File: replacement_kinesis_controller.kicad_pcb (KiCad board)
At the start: 2 copper layers, 99.1 x 99.1 mm, 138 parts, among them CN1 USB_general, CN2 Micro-USB, CN3 Mini-USB, CN4 USB_general, K1 CONN_3, K2 CONN_3, K3 CONN_3, K4 CONN_3, K5 CONN_3, P1 CONN_3X2, P10 CONN_8, P11 CONN_5, P12 CONN_5, P13 CONN_6, P14 CONN_8, P15 CONN_5X2, P16 CONN_16, P17 CONN_16, P18 POWER, P19 PCM, P2 CONN_13, P20 UART, P21 SPI, P22 IO, P23 SMIRF, P24 CONN_2, P25 USB, P3 CONN_13, P4 CONN_10, P5 CONN_10, P6 CONN_13, P7 CONN_13, P8 CONN_5X2, P9 CONN_6, Q1 MOS_P, Q2 MOS_N, Q3 MOS_P, SW1 SW_PUSH, SW2 SW_PUSH, SW3 SPST, SW4 SPST, U1 MCP23018-E, U2 WS2811_RGB_LED, U3 WS2811_RGB_LED, U4 WS2811_RGB_LED, U5 WS2811_RGB_LED, U6 ATmega32U4, U7 WT12-A, U8 MCP73832, U9 MIC5504, X1 16MHz

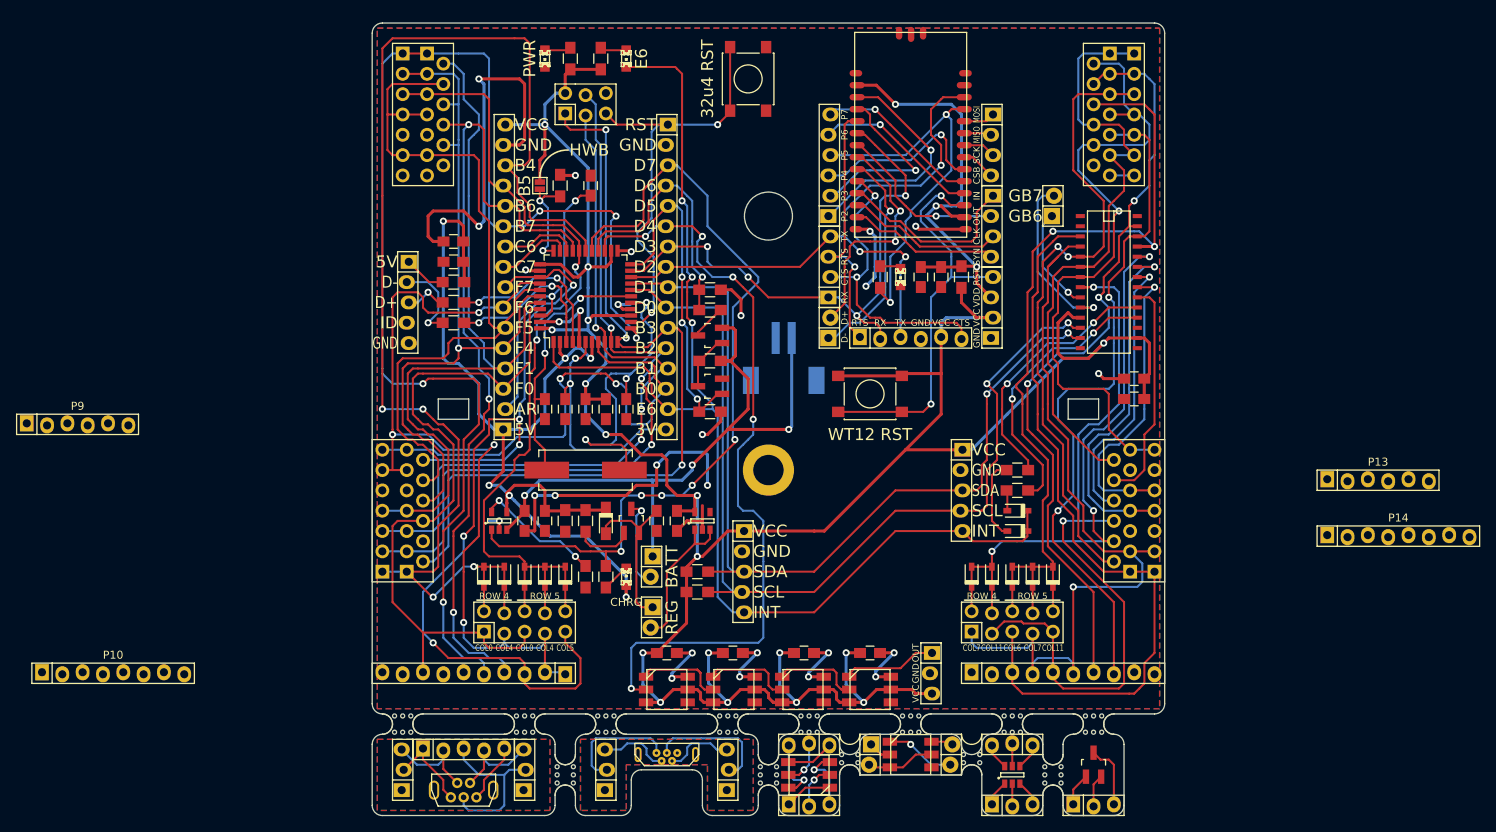
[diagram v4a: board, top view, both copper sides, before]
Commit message: Rejigger things to make board more easily separable
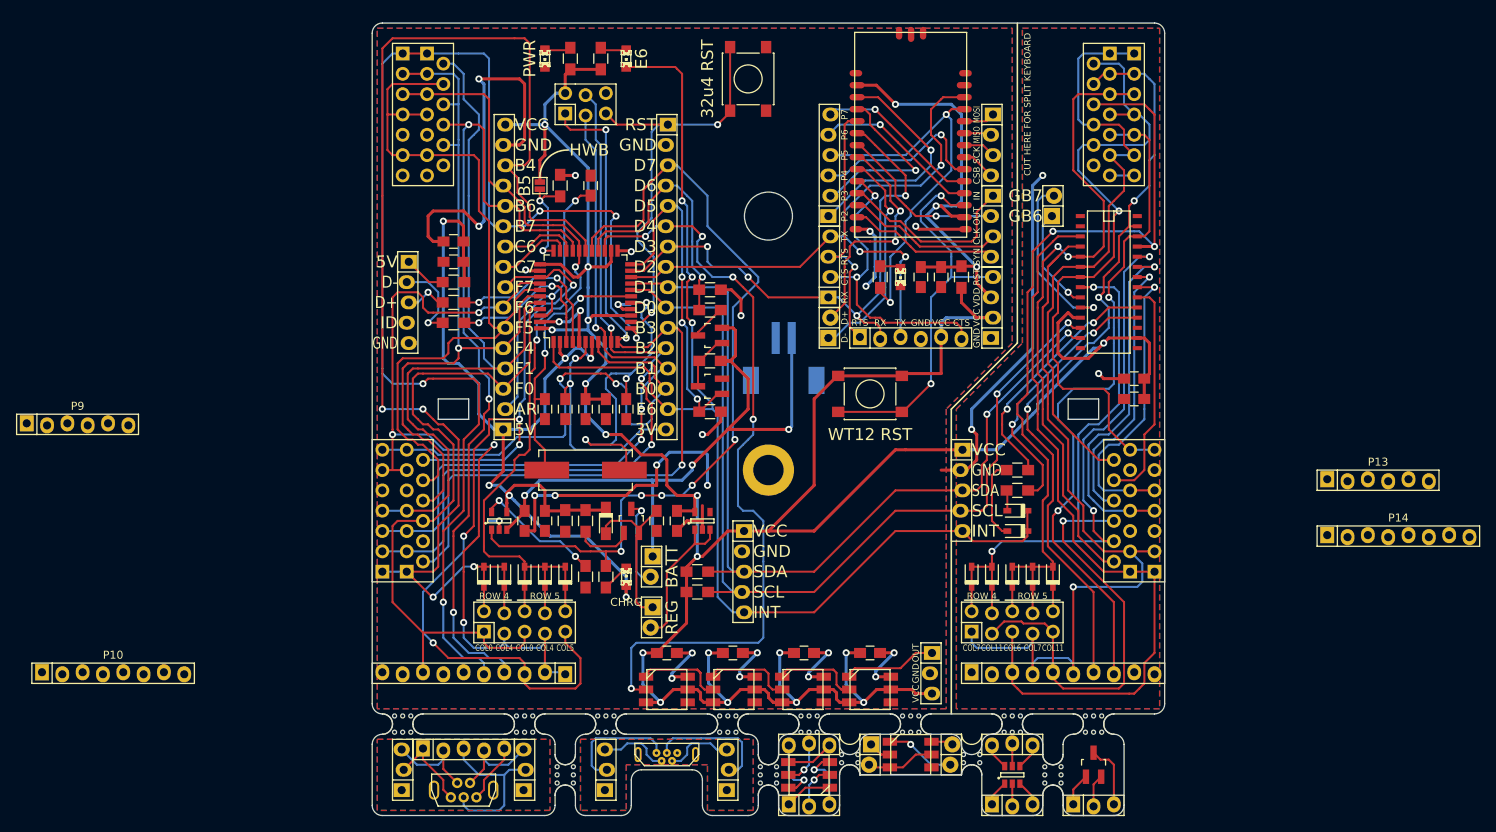
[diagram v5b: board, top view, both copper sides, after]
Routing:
- net GND: track 169.0 -> 213.5 mm, vias 27 -> 29
- net VCC: track 352.5 -> 364.6 mm
- net PD0: track 120.0 -> 117.5 mm
- net SDA: track 114.7 -> 113.2 mm
- net GPA7: track 96.7 -> 95.2 mm
- net W_RESET: track 51.6 -> 50.1 mm
- net INTB: track 35.0 -> 33.5 mm
- net INTA: track 32.6 -> 31.1 mm
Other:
- board text added: "CUT HERE FOR SPLIT KEYBOARD"

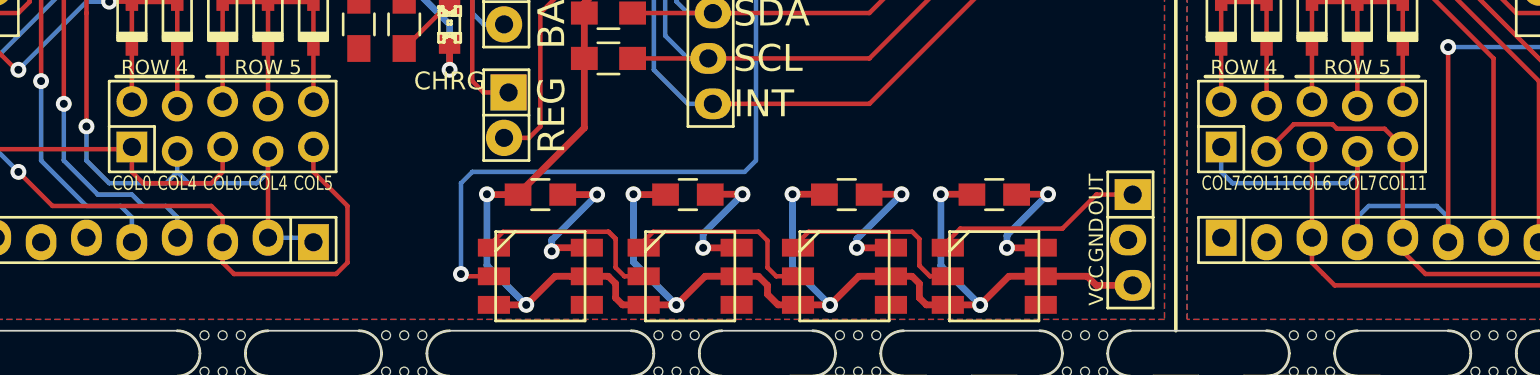
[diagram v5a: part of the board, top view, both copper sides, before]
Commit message: A bunch of silkscreen improvements
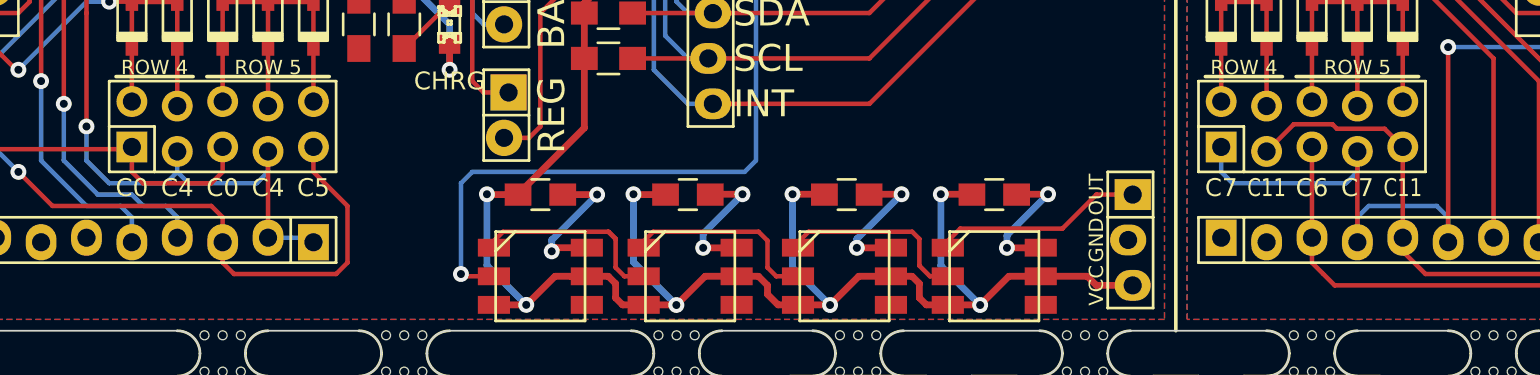
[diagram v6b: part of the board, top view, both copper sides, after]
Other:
- board text added: "C0"
- board text added: "C11"
- board text added: "C4"
- board text added: "C5"
- board text removed: "COL0"
- board text removed: "COL11"
- board text removed: "COL4"
- board text removed: "COL5"
- board text removed: "COL6"
- board text removed: "COL7"

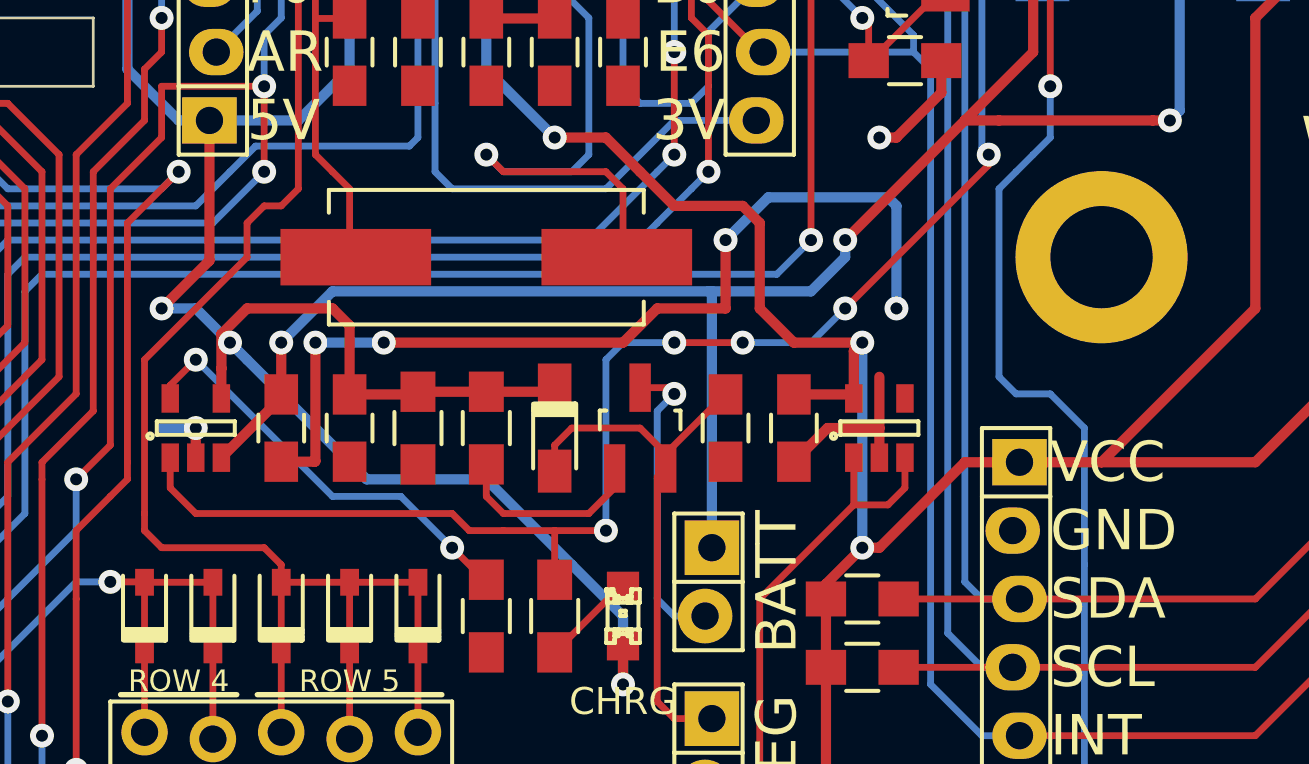
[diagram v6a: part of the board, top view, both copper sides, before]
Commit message: Update sot23-5 footprint for handsoldering
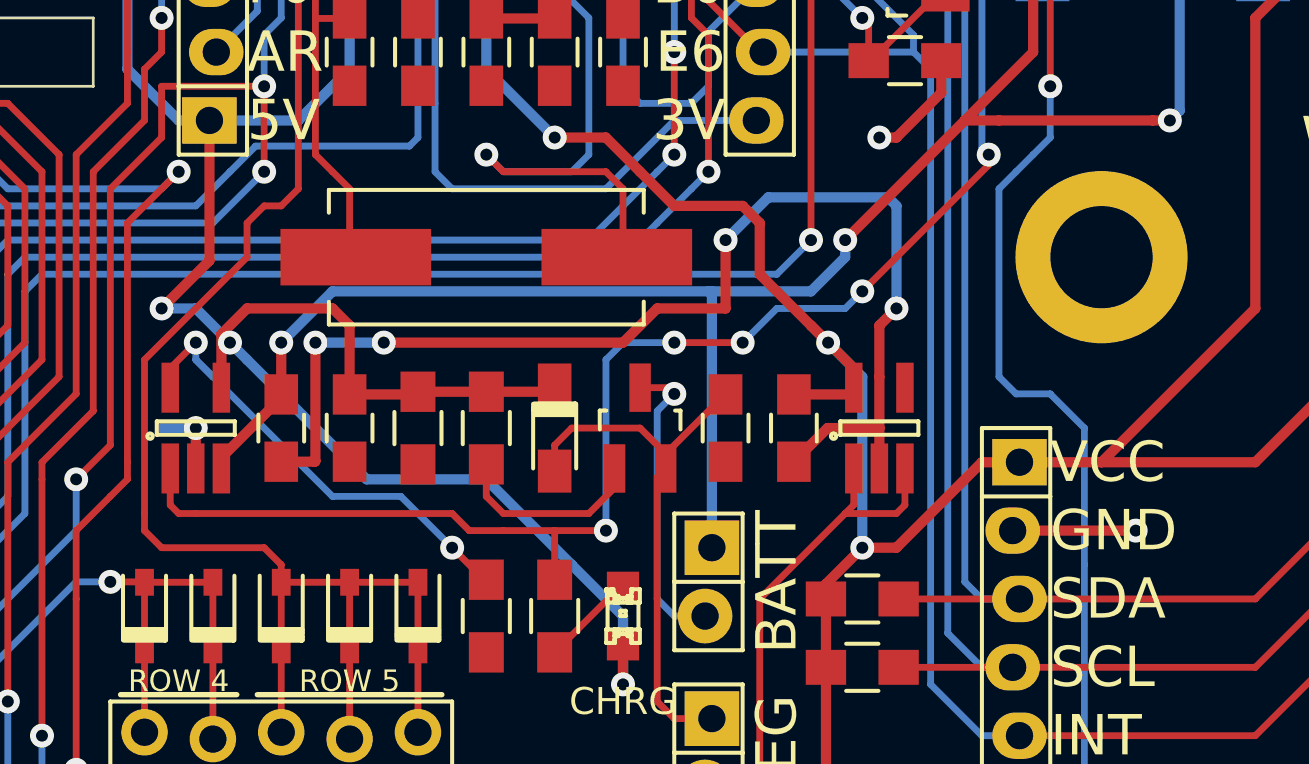
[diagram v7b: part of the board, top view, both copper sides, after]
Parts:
- U8, U9: footprint Housings_SOT-23_SOT-143_TSOT-6:SOT23-5 -> replacement_kinesis_controller:SOT23-5_handsolder
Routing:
- net GND: track 213.5 -> 220.8 mm, vias 29 -> 30
- net Net-(R18-Pad1): track 16.0 -> 18.7 mm
- net Net-(SW4-Pad2): track 18.6 -> 20.6 mm
- net PD7: track 101.9 -> 103.4 mm

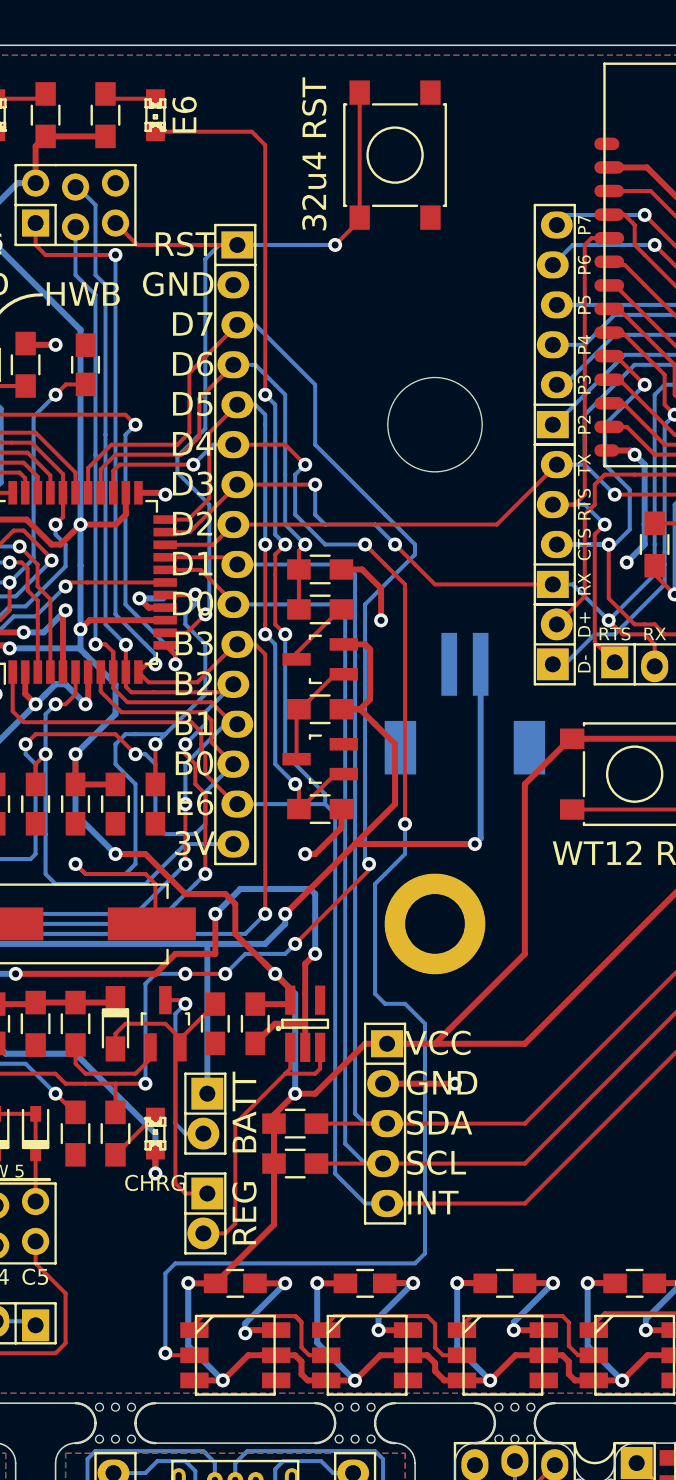
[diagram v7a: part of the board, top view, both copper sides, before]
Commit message: More silk updates and another WS2811 breakout
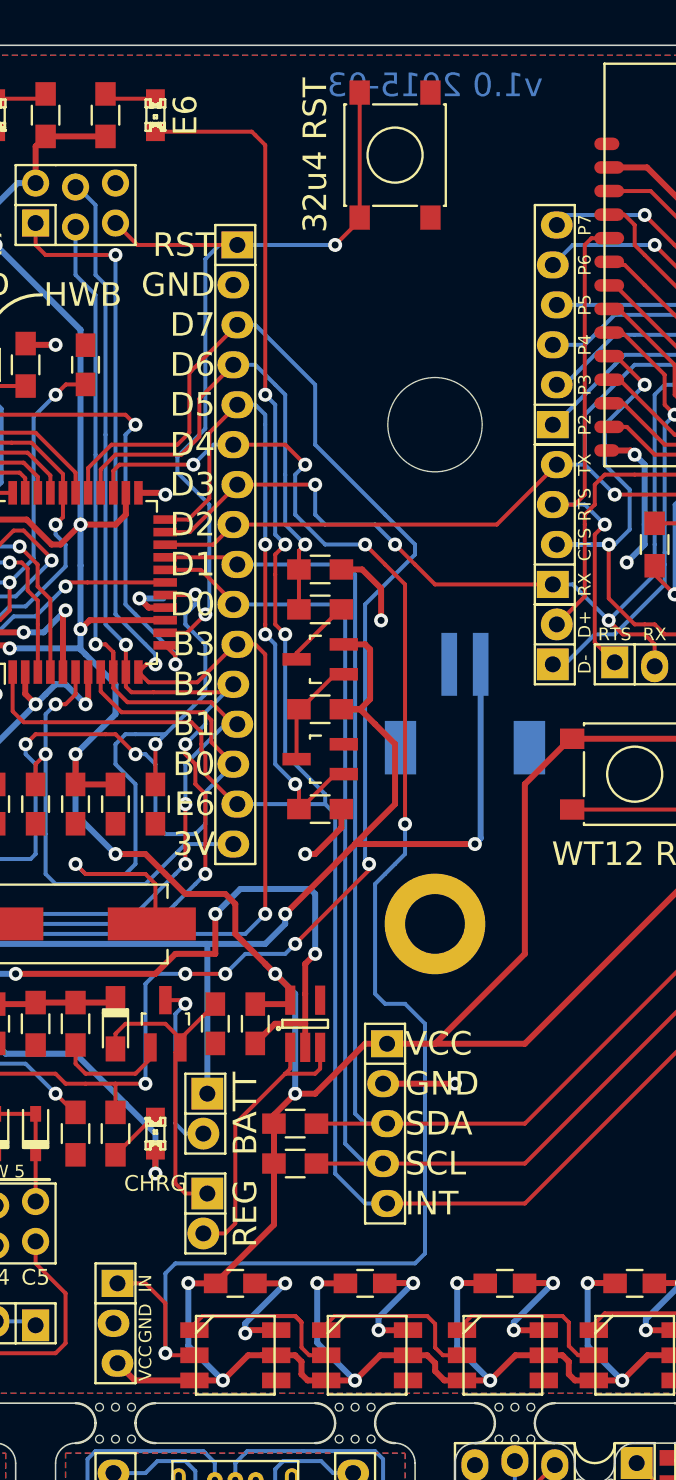
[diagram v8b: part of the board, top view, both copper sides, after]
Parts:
- added G***: LOGO, replacement_kinesis_controller:oshw-logo, B.Cu at (90.2, 48.9)
- added K5: CONN_3, replacement_kinesis_controller:Pin_Header_Staggered_Straight_1x03, F.Cu at (102.9, 124.5)
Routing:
- net PD4: track 96.5 -> 103.2 mm
- net VCC: track 364.3 -> 369.6 mm
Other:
- board text added: "v1.0 2015-03"
